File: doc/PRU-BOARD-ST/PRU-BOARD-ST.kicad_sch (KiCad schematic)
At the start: 23 parts, among them J1 Conn_02x20_Odd_Even, J2 Conn_01x10, J3 Conn_01x06, Q1 BC817, U1 STM32F103C6Tx, U2 MCP6L02x-xSN, U3 LTV-817, U4 LTV-817, U5 LTV-817, U6 LTV-817, U7 AMS1117-3.3, U8 74HCT541, Y1 12MHz

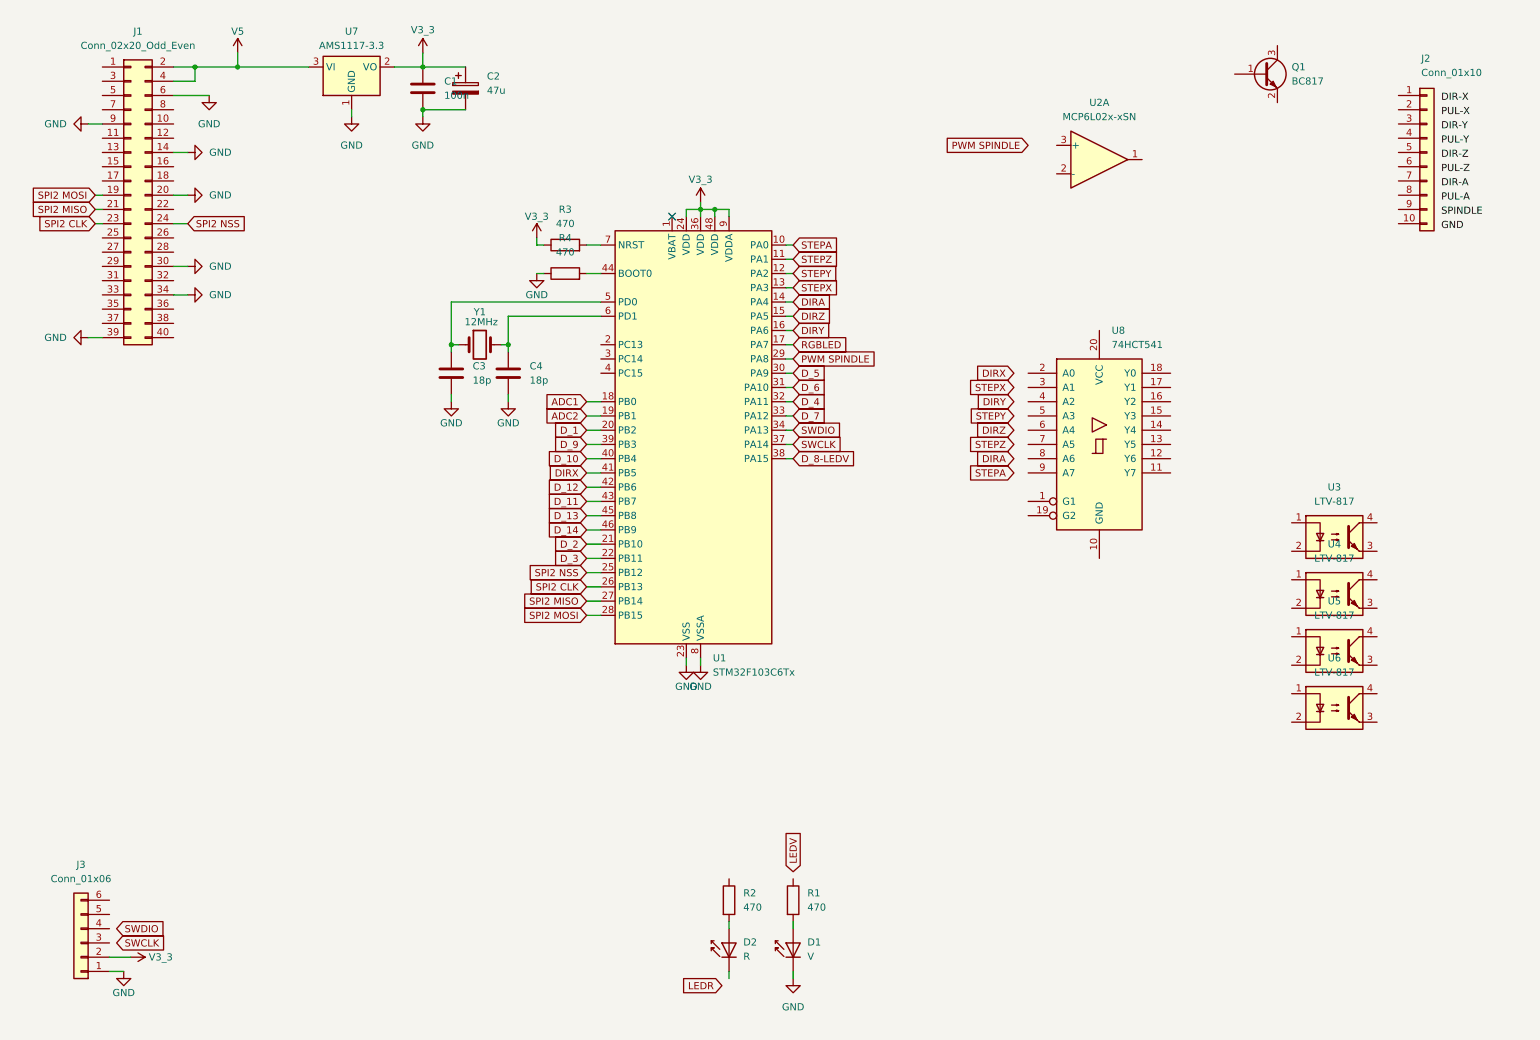
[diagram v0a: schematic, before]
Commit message: Blocco mandrino
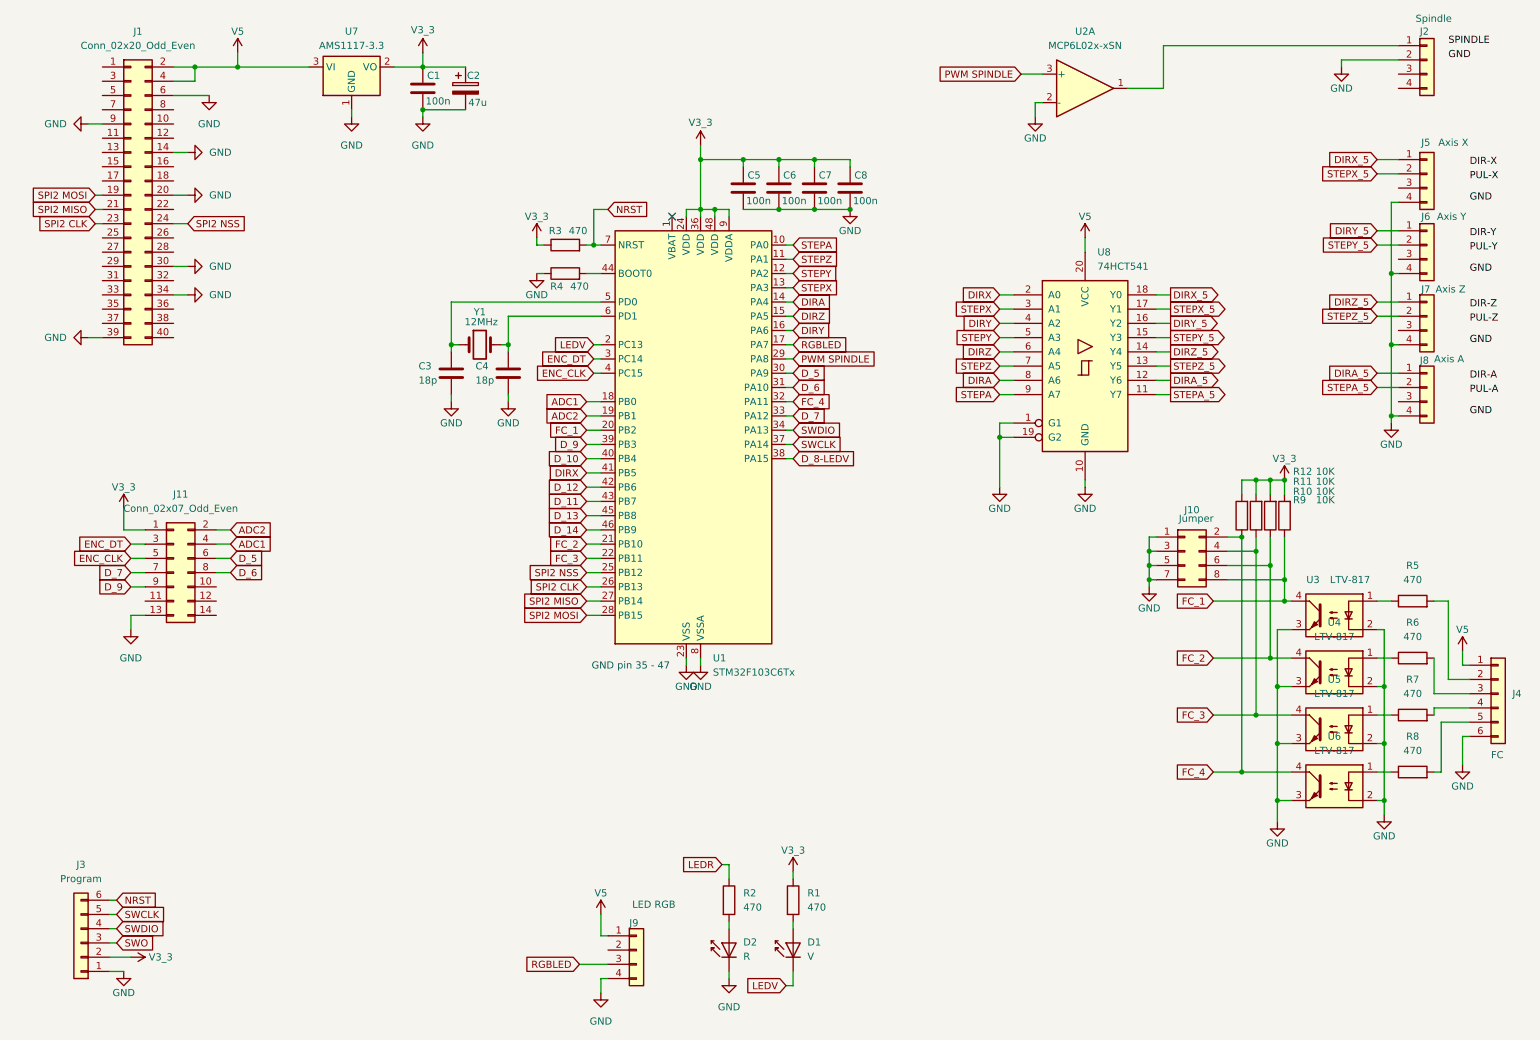
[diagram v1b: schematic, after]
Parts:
- removed J2: Conn_01x10, symbol Connector_Generic:Conn_01x10
- removed Q1: BC817, Package_TO_SOT_SMD:SOT-23, symbol Transistor_BJT:BC817
- added C5, C6, C7, C8: 100n, symbol Device:C
- added J10: Jumper, symbol Connector_Generic:Conn_02x04_Odd_Even
- added J11: Conn_02x07_Odd_Even, symbol Connector_Generic:Conn_02x07_Odd_Even
- added J2: Spindle, symbol Connector_Generic:Conn_01x04
- added J4: FC, symbol Connector_Generic:Conn_01x06
- added J5: Axis X, symbol Connector_Generic:Conn_01x04
- added J6: Axis Y, symbol Connector_Generic:Conn_01x04
- added J7: Axis Z, symbol Connector_Generic:Conn_01x04
- added J8: Axis A, symbol Connector_Generic:Conn_01x04
- added J9: LED RGB, symbol Connector_Generic:Conn_01x04
- added R10, R11, R12, R9: 10K, symbol Device:R
- added R5, R6, R7, R8: 470, symbol Device:R
- J3: value Conn_01x06 -> Program
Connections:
- net D_1 is gone; now on net FC_1: U1.20 (PB2)
- net D_2 is gone; now on net FC_2: U1.21 (PB10)
- net D_3 is gone; now on net FC_3: U1.22 (PB11)
- net D_4 is gone; now on net FC_4: U1.32 (PA11)
- net ADC1: now also J11.4 (Pin_4)
- net ADC2: now also J11.2 (Pin_2)
- net DIRA: now also U8.8 (A6)
- net DIRX: now also U8.2 (A0)
- net DIRY: now also U8.4 (A2)
- net DIRZ: now also U8.6 (A4)
- net D_5: now also J11.6 (Pin_6)
- net D_6: now also J11.8 (Pin_8)
- net D_7: now also J11.7 (Pin_7)
- net D_9: now also J11.9 (Pin_9)
- net GND: now also D2.1 (K), U2.2 (-), U3.2, U3.3, U4.2, U4.3, U5.2, U5.3, U6.2, U6.3, U8.1 (G1), U8.10 (GND), U8.19 (G2), C5.2, C6.2, C7.2, C8.2, J10.1 (Pin_1), J10.3 (Pin_3), J10.5 (Pin_5), J10.7 (Pin_7), J11.13 (Pin_13), J2.2 (Pin_2), J4.6 (Pin_6), J5.4 (Pin_4), J6.4 (Pin_4), J7.4 (Pin_4), J8.4 (Pin_4), J9.4 (Pin_4); no longer D1.1 (K)
- net LEDR: now also R2.1
- net LEDV: now also D1.1 (K), U1.2 (PC13)
- net PWM SPINDLE: now also U2.3 (+)
- net RGBLED: now also J9.3 (Pin_3)
- net STEPA: now also U8.9 (A7)
- net STEPX: now also U8.3 (A1)
- net STEPY: now also U8.5 (A3)
- net STEPZ: now also U8.7 (A5)
- net SWCLK: now also J3.5 (Pin_5)
- net SWDIO: now also J3.4 (Pin_4)
- net V3_3: now also R1.1, C5.1, C6.1, C7.1, C8.1, J11.1 (Pin_1), R10.2, R11.2, R12.2, R9.2
- net V5: now also U8.20 (VCC), J4.1 (Pin_1), J9.1 (Pin_1)
- net at U6.1: now also R8.1
- net FC_4: now reaches U6.4
- net FC_4: now also J10.2 (Pin_2), R12.1
- net at U2.1: now also J2.1 (Pin_1)
- net ENC_DT: now reaches U1.3 (PC14)
- net ENC_DT: now also J11.3 (Pin_3)
- net ENC_CLK: now reaches U1.4 (PC15)
- net ENC_CLK: now also J11.5 (Pin_5)
- net NRST: now reaches R3.2, U1.7 (NRST)
- net NRST: now also J3.6 (Pin_6)
- net at U4.1: now also R6.1
- net FC_2: now reaches U4.4
- net FC_2: now also J10.6 (Pin_6), R10.1
- net at U3.1: now also R5.1
- net FC_1: now reaches U3.4
- net FC_1: now also J10.8 (Pin_8), R9.1
- net at U5.1: now also R7.1
- net FC_3: now reaches U5.4
- net FC_3: now also J10.4 (Pin_4), R11.1
- net SWO: now reaches J3.3 (Pin_3)
- net STEPA_5: now reaches U8.11 (Y7)
- net STEPA_5: now also J8.2 (Pin_2)
- net DIRA_5: now reaches U8.12 (Y6)
- net DIRA_5: now also J8.1 (Pin_1)
- net STEPZ_5: now reaches U8.13 (Y5)
- net STEPZ_5: now also J7.2 (Pin_2)
- net DIRZ_5: now reaches U8.14 (Y4)
- net DIRZ_5: now also J7.1 (Pin_1)
- net STEPY_5: now reaches U8.15 (Y3)
- net STEPY_5: now also J6.2 (Pin_2)
- net DIRY_5: now reaches U8.16 (Y2)
- net DIRY_5: now also J6.1 (Pin_1)
- net STEPX_5: now reaches U8.17 (Y1)
- net STEPX_5: now also J5.2 (Pin_2)
- net DIRX_5: now reaches U8.18 (Y0)
- net DIRX_5: now also J5.1 (Pin_1)
- new net: J4.4 (Pin_4), R7.2
- new net: J4.5 (Pin_5), R8.2
- new net: J4.3 (Pin_3), R6.2
- new net: J4.2 (Pin_2), R5.2
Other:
- note added: "GND pin 35 - 47"
- title: (none) -> GRBL - CNC -ST
- moved on the sheet: U2A, U3, U4, U5, U6, U8

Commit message: schema - accessori tappo maniglia audi
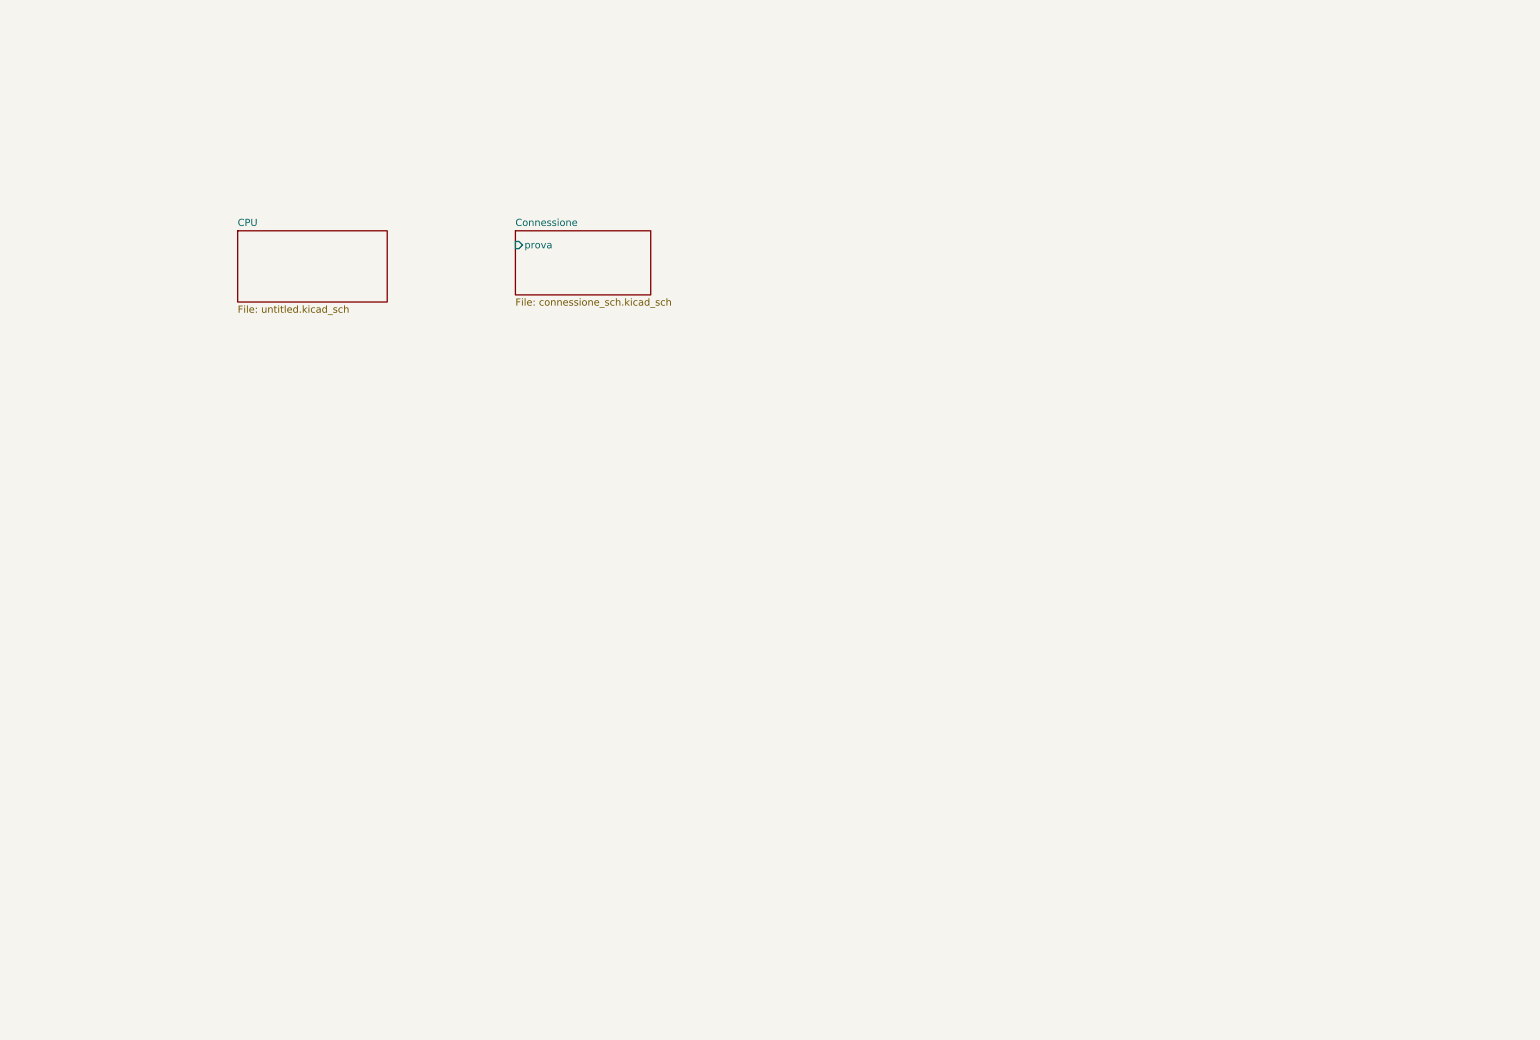
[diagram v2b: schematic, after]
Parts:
- removed C1, C5, C6, C7, C8: 100n, symbol Device:C
- removed C2: 47u, symbol Device:C_Polarized
- removed C3, C4: 18p, symbol Device:C
- removed D1: V, Package_TO_SOT_THT:TO-18-2_Window, symbol LED:SFH460
- removed D2: R, Package_TO_SOT_THT:TO-18-2_Window, symbol LED:SFH460
- removed J1: Conn_02x20_Odd_Even, symbol Connector_Generic:Conn_02x20_Odd_Even
- removed J10: Jumper, symbol Connector_Generic:Conn_02x04_Odd_Even
- removed J11: Conn_02x07_Odd_Even, symbol Connector_Generic:Conn_02x07_Odd_Even
- removed J2: Spindle, symbol Connector_Generic:Conn_01x04
- removed J3: Program, symbol Connector_Generic:Conn_01x06
- removed J4: FC, symbol Connector_Generic:Conn_01x06
- removed J5: Axis X, symbol Connector_Generic:Conn_01x04
- removed J6: Axis Y, symbol Connector_Generic:Conn_01x04
- removed J7: Axis Z, symbol Connector_Generic:Conn_01x04
- removed J8: Axis A, symbol Connector_Generic:Conn_01x04
- removed J9: LED RGB, symbol Connector_Generic:Conn_01x04
- removed R1, R2, R3, R4, R5, R6, R7, R8: 470, symbol Device:R
- removed R10, R11, R12, R9: 10K, symbol Device:R
- removed U1: STM32F103C6Tx, Package_QFP:LQFP-48_7x7mm_P0.5mm, symbol MCU_ST_STM32F1:STM32F103C6Tx
- removed U2: MCP6L02x-xSN, Package_SO:SOIC-8_3.9x4.9mm_P1.27mm, symbol Amplifier_Operational:MCP6L02x-xSN
- removed U3, U4, U5, U6: LTV-817, Package_DIP:DIP-4_W7.62mm, symbol Isolator:LTV-817
- removed U7: AMS1117-3.3, Package_TO_SOT_SMD:SOT-223-3_TabPin2, symbol Regulator_Linear:AMS1117-3.3
- removed U8: 74HCT541, symbol 74xx:74HCT541
- removed Y1: 12MHz, symbol Device:Crystal
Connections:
- no-connect marks 1 -> 0
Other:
- added sheet CPU (untitled.kicad_sch)
- added sheet Connessione (connessione_sch.kicad_sch)
- note removed: "GND pin 35 - 47"

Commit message: maggio2025
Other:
- sheet Connessione renamed Connection_InverterSpindle
- added sheet IO_connection (IO_connection.kicad_sch)
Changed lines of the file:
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@@
 			(color 0 0 0 0.0000)
 		)
-		(property "Sheetname" "Connessione"
+		(property "Sheetname" "Connection_InverterSpindle"
 			(at 102.87 51.3584 0)
 			(effects
@@
 				)
 			)
+		)
+	)
+	(sheet
+		(at 156.21 50.8)
+		(size 24.13 11.43)
+		(exclude_from_sim no)
+		(in_bom yes)
+		(on_board yes)
+		(dnp no)
+		(fields_autoplaced yes)
+		(stroke
+			(width 0.1524)
+			(type solid)
+		)
+		(fill
+			(color 0 0 0 0.0000)
+		)
+		(property "Sheetname" "IO_connection"
+			(at 156.21 50.0884 0)
+			(effects
+				(font
+					(size 1.27 1.27)
+				)
+				(justify left bottom)
+			)
+		)
+		(property "Sheetfile" "IO_connection.kicad_sch"
+			(at 156.21 62.8146 0)
+			(effects
+				(font
+					(size 1.27 1.27)
+				)
+				(justify left top)
+			)
+		)
+		(instances
+			(project "PRU-BOARD-ST"
+				(path "/83376baa-8092-4242-8be4-15446c519f68"
+					(page "4")
+				)
+			)
